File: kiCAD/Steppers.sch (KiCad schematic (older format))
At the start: 108 parts

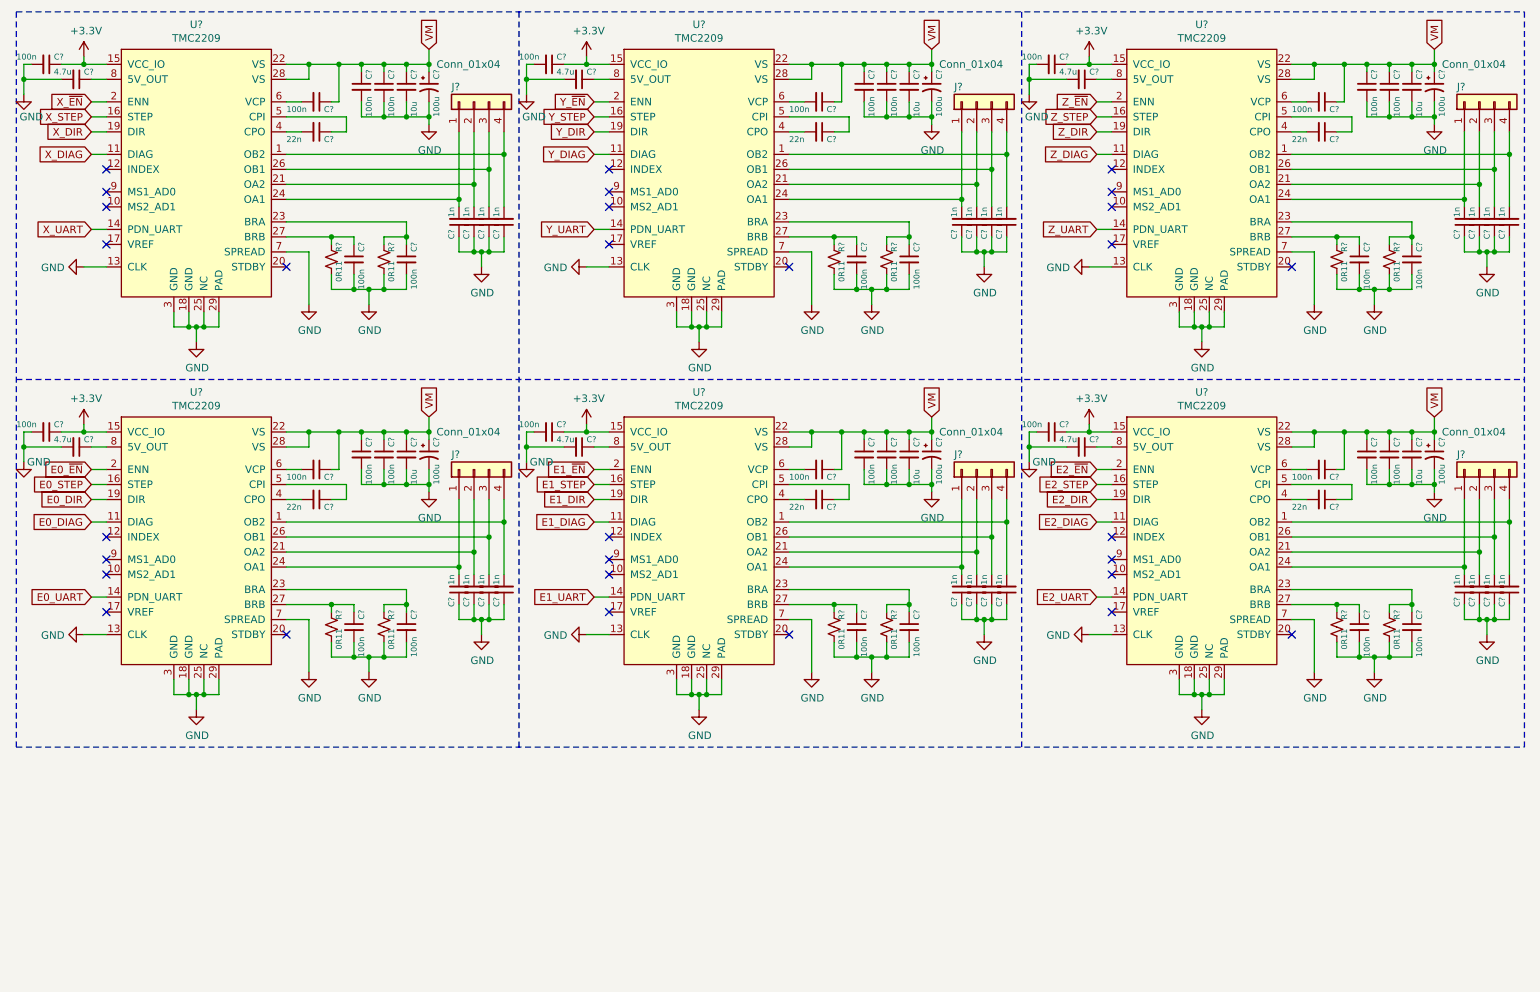
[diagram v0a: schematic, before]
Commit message: Completed Schematic, assigned footprints.
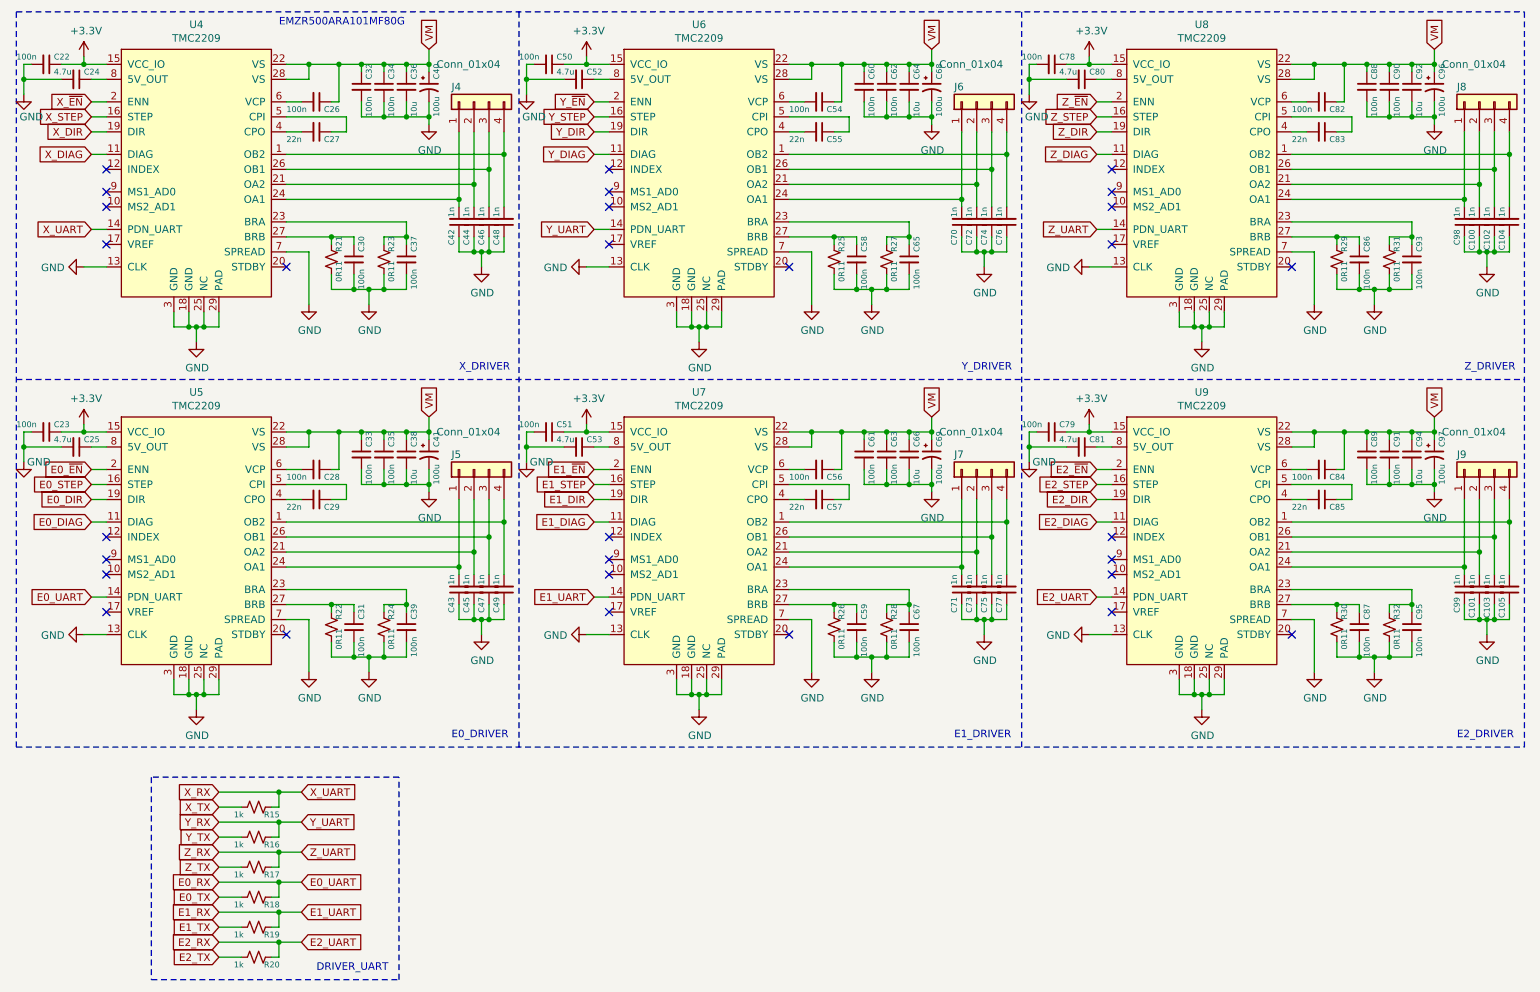
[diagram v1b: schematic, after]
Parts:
- added R15, R16, R17, R18, R19, R20: 1k, Resistor_SMD:R_0603_1608Metric_Pad1.05x0.95mm_HandSolder, symbol Device:R_Small_US
- C100, C101, C102, C103, C104, C105, C22, C23, C24, C25, C26, C27, C28, C29, C30, C31, C32, C33, C34, C35, C37, C39, C42, C43, C44, C45, C46, C47, C48, C49, C50, C51, C52, C53, C54, C55, C56, C57, C58, C59, C60, C61, C62, C63, C65, C67, C70, C71, C72, C73, C74, C75, C76, C77, C78, C79, C80, C81, C82, C83, C84, C85, C86, C87, C88, C89, C90, C91, C93, C95, C98, C99: renamed from C?; footprint (none) -> Capacitor_SMD:C_0603_1608Metric_Pad1.05x0.95mm_HandSolder
- C36, C38, C64, C66, C92, C94: renamed from C?; footprint (none) -> Capacitor_SMD:C_1206_3216Metric_Pad1.42x1.75mm_HandSolder
- C40, C41, C68, C69, C96, C97: renamed from C?; footprint (none) -> Capacitor_SMD:CP_Elec_6.3x7.7
- J4, J5, J6, J7, J8, J9: renamed from J?; footprint (none) -> Connector_Molex:Molex_KK-254_AE-6410-04A_1x04_P2.54mm_Vertical
- R21, R22, R23, R24, R25, R26, R27, R28, R29, R30, R31, R32: renamed from R?; footprint (none) -> Resistor_SMD:R_0805_2012Metric_Pad1.15x1.40mm_HandSolder
- U4, U5, U6, U7, U8, U9: renamed from U?; footprint (none) -> Package_DFN_QFN:QFN-28-1EP_5x5mm_P0.5mm_EP3.35x3.35mm_ThermalVias
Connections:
- net E0_UART renamed E0_RX
- net E0_RX: now also R18.1
- net E1_UART renamed E1_RX
- net E1_RX: now also R19.1
- net E2_UART renamed E2_RX
- net E2_RX: now also R20.1
- net X_UART renamed X_RX
- net X_RX: now also R15.1
- net Y_UART renamed Y_RX
- net Y_RX: now also R16.1
- net Z_UART renamed Z_RX
- net Z_RX: now also R17.1
- new net E0_TX: R18.2
- new net E1_TX: R19.2
- new net E2_TX: R20.2
- new net X_TX: R15.2
- new net Y_TX: R16.2
- new net Z_TX: R17.2
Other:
- note added: "DRIVER_UART\n"
- note added: "E0_DRIVER\n"
- note added: "E1_DRIVER\n"
- note added: "E2_DRIVER\n"
- note added: "EMZR500ARA101MF80G"
- note added: "X_DRIVER\n"
- note added: "Y_DRIVER"
- note added: "Z_DRIVER\n"
